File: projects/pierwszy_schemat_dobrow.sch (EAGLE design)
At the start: 30 parts, among them IC1 74HC595N, IC2 7805T, U2 ARDUINOR3-DIMENSION

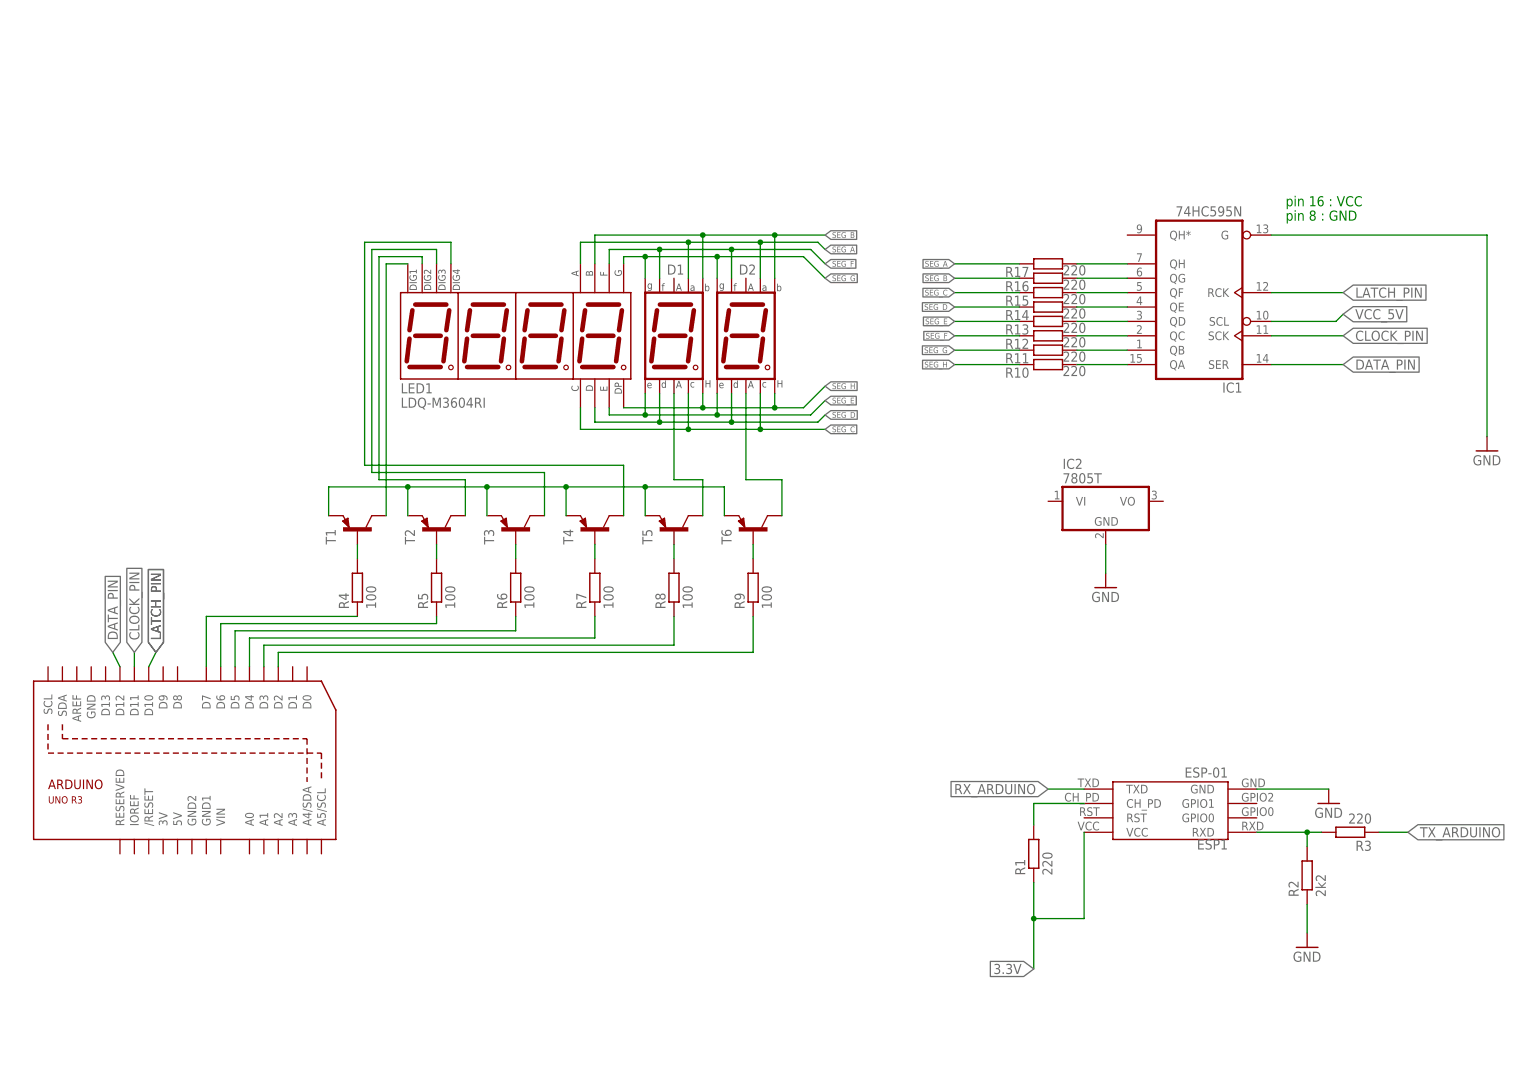
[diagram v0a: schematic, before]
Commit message: completed lm7805 schematics
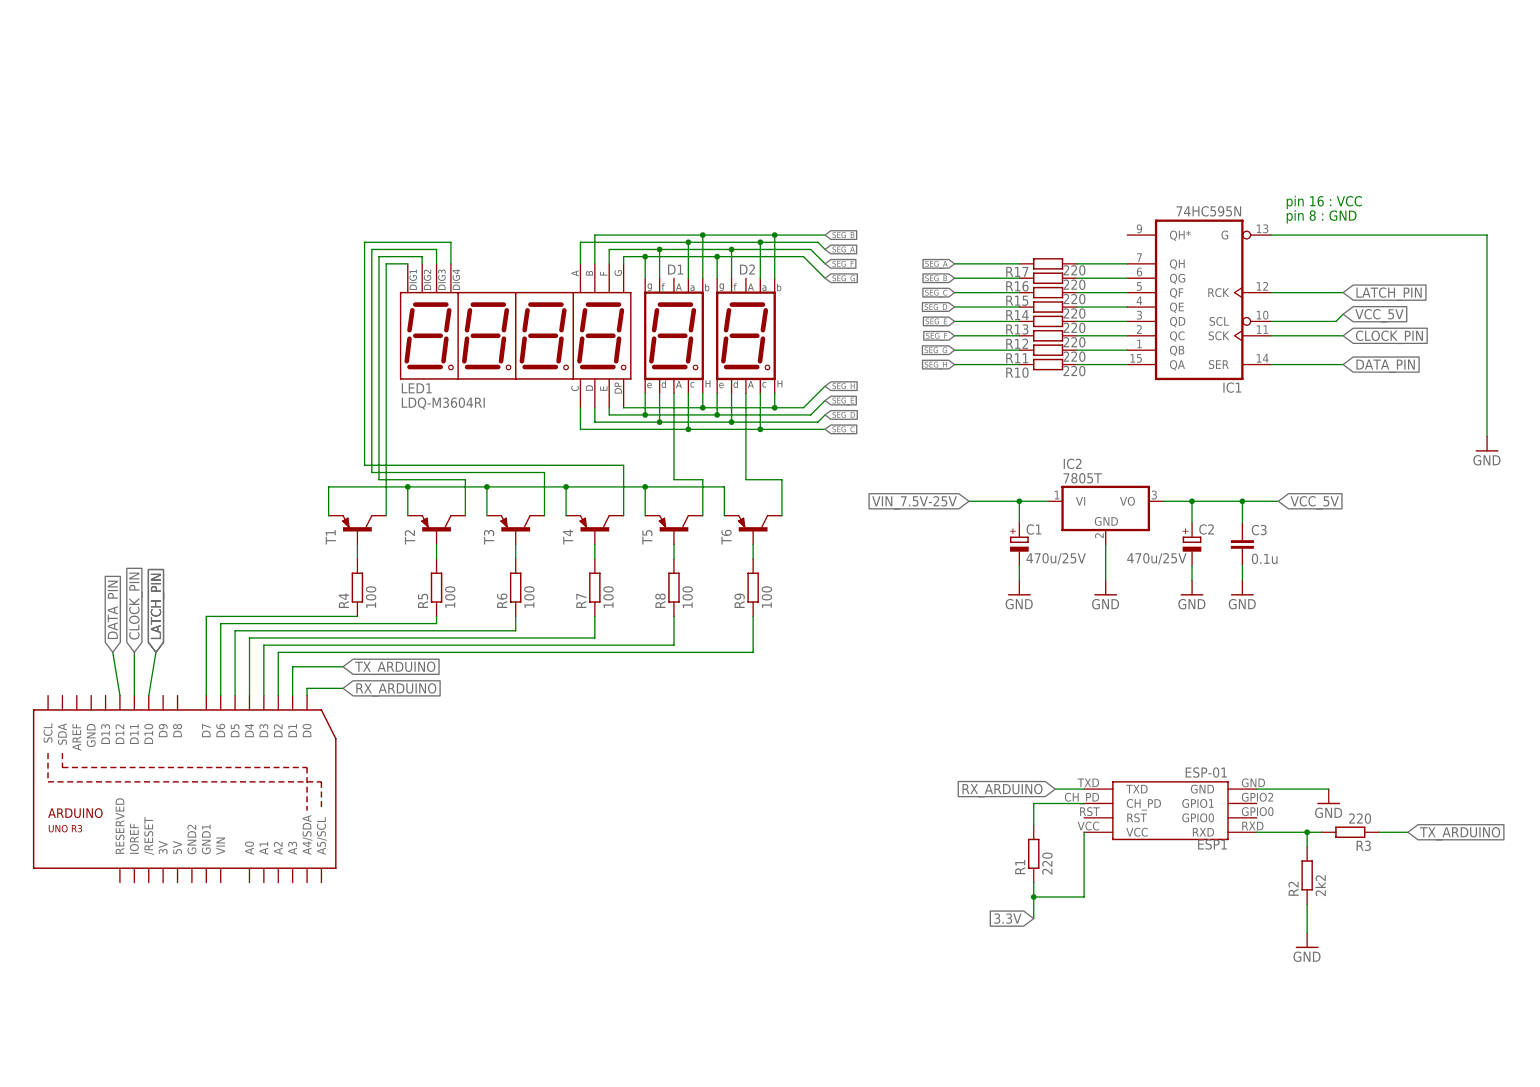
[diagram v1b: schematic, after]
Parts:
- added C1, C2: 470u/25V, rcl:CPOL-EUE5-8.5
- added C3: 0.1u, rcl:C-EU025-025X050
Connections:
- new net N$11: C1.-
- new net N$21: C2.-
- new net VIN_7.5V-25V: C1.+, IC2.VI
- net GND: now also C3.2
- net RX_ARDUINO: now also U2.D0
- net TX_ARDUINO: now also U2.D1
- net VCC_5V: now also C2.+, C3.1, IC2.VO

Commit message: added 3v3voltage regulator and rearanged
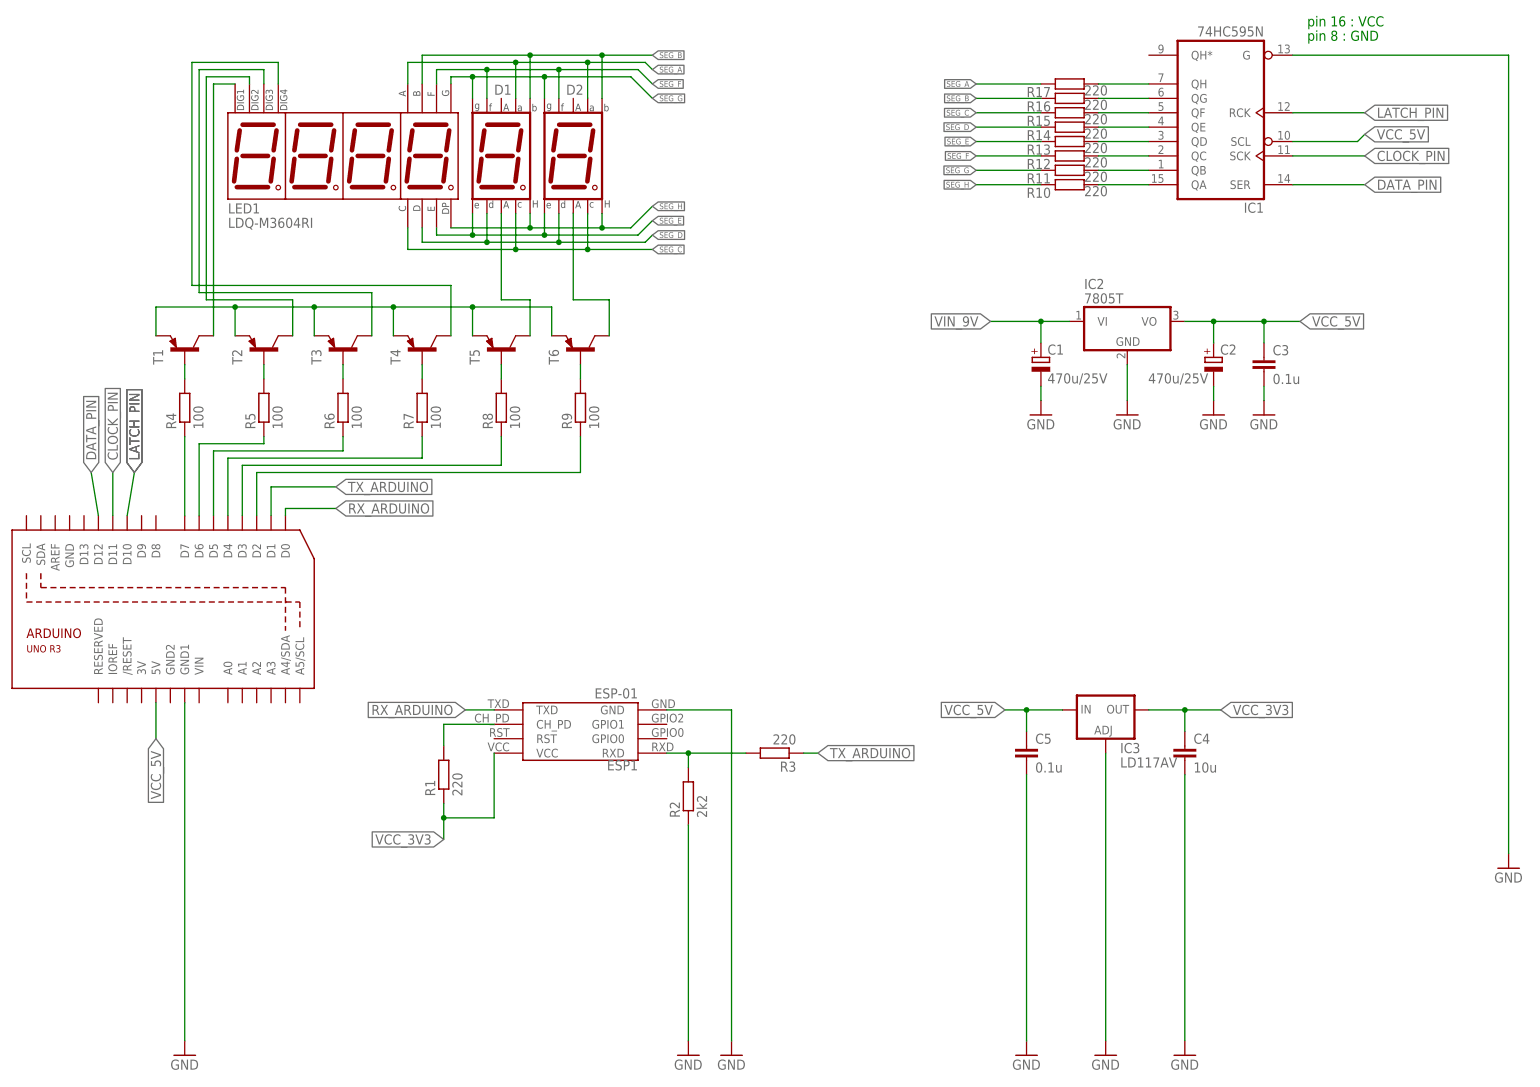
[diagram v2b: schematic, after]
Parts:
- added C4: 10u, rcl:C-EU025-025X050
- added C5: 0.1u, rcl:C-EU025-025X050
- added IC3: LD117AV, v-reg:LD117AV
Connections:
- net VIN_7.5V-25V renamed VIN_9V
- removed net 3.3V: ESP1.VCC, R1.1
- new net N$20: U2.GND1
- new net VCC_3V3: C4.1, ESP1.VCC, IC3.OUT, R1.1
- net GND: now also C4.2, C5.2, IC3.ADJ
- net VCC_5V: now also C5.1, IC3.IN, U2.5V
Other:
- moved on the sheet: C1, C2, C3, D1, D2, ESP1, IC1, IC2, LED1, R1, R10, R11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
